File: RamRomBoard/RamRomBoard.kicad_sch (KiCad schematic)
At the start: 84 parts, among them J10 Micro_SD_Card_Det2, J5 Screw_Terminal_01x02, J6 USB_B_Micro, J7 STM32F401, J8 Dual LED Socket, J9 JTAG, SW1 033TBVSA, SW2 SW_Push, U1 74LVC125, U10 74AHC1G14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

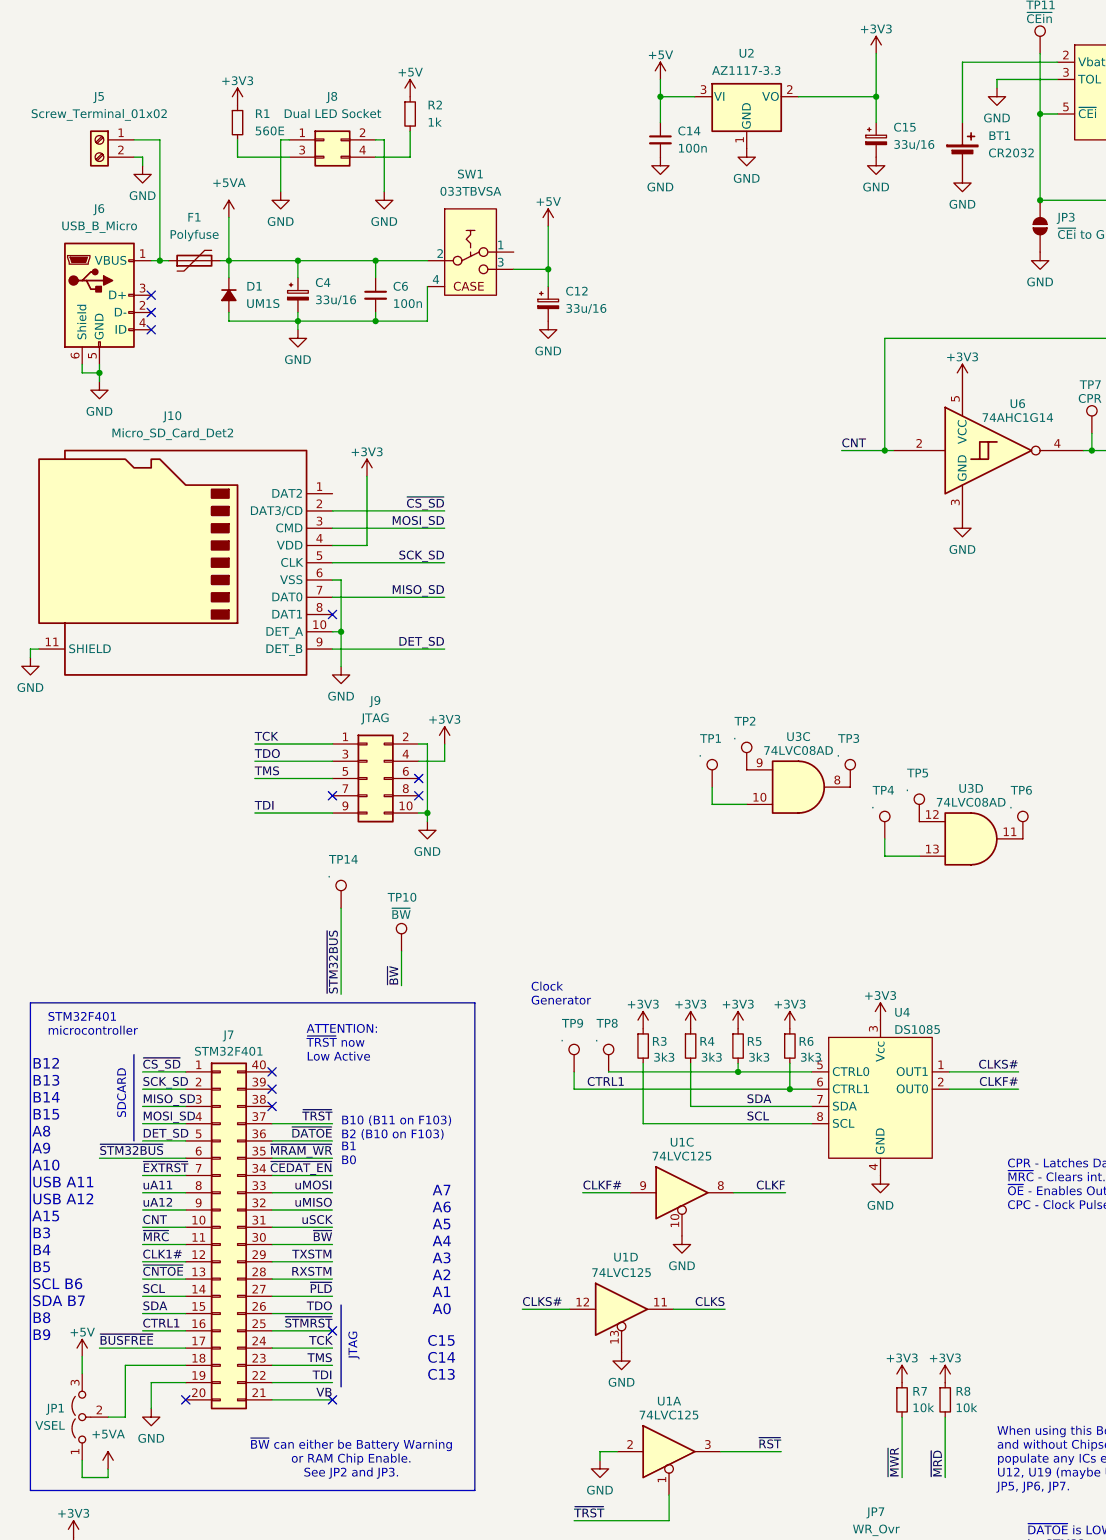
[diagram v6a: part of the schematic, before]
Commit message: first boards manufactured
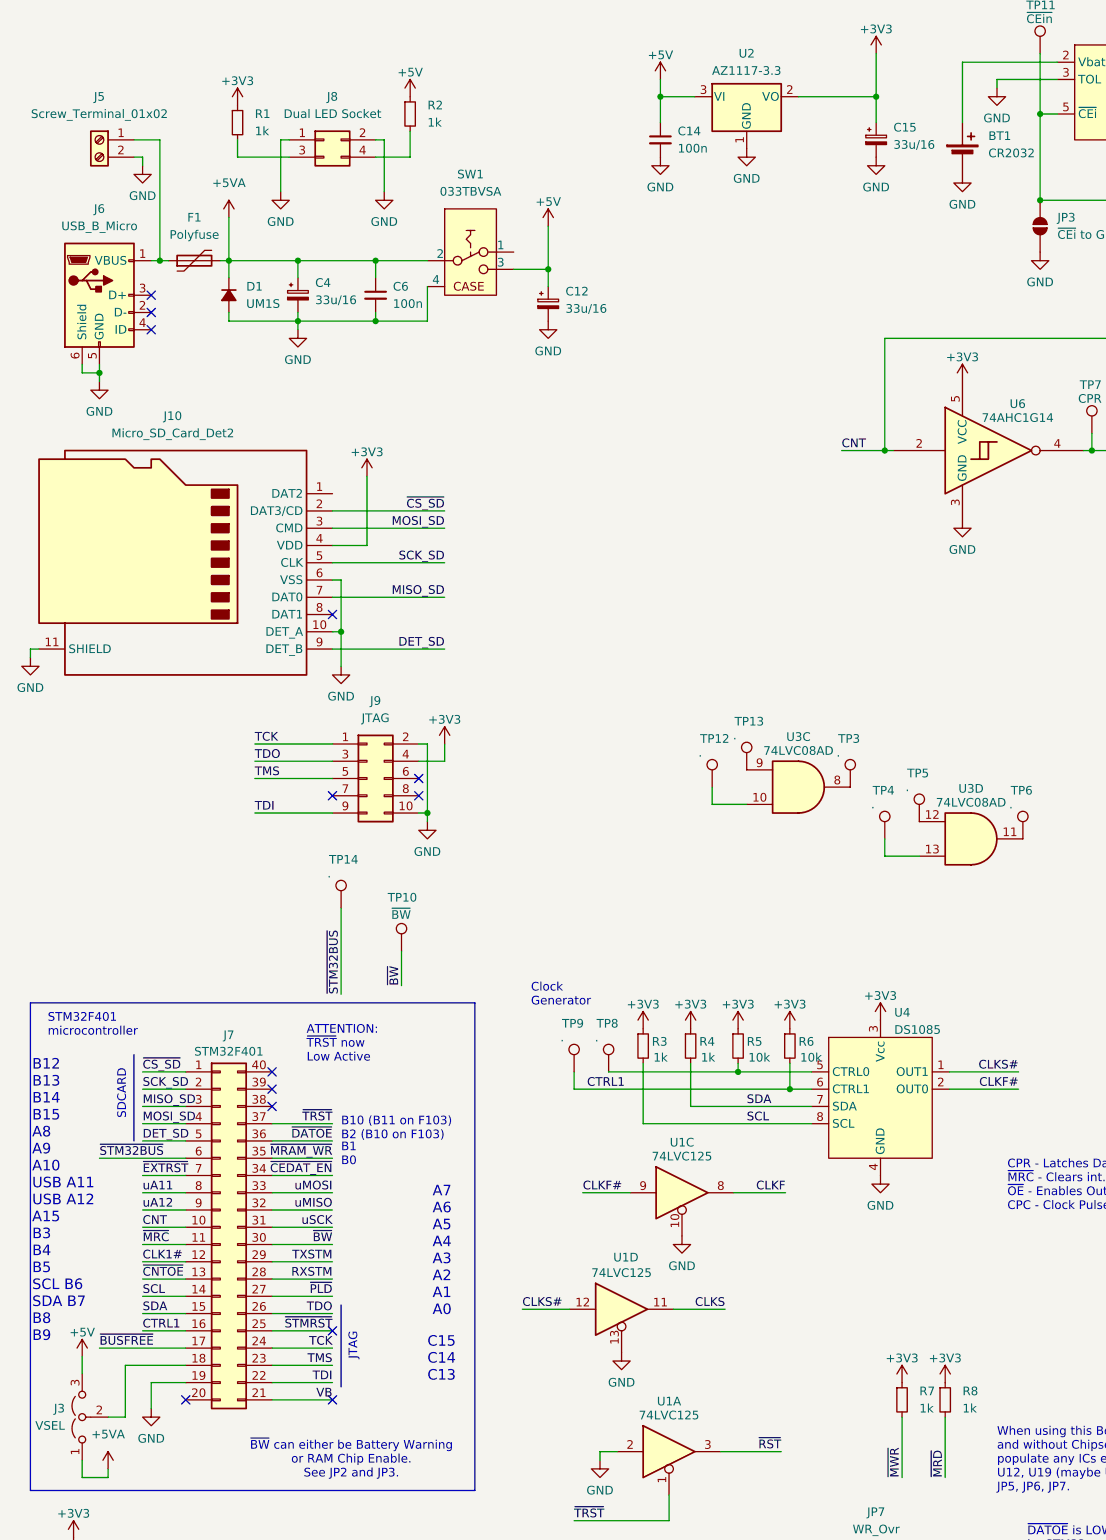
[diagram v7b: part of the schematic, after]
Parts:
- J3: renamed from JP1; now in the parts list
- R1: value 560E -> 1k
- R3, R4: value 3k3 -> 1k
- R5, R6: value 3k3 -> 10k
- R7, R8: value 10k -> 1k
- renumbered TP1 to TP12, TP2 to TP13
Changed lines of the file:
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@@
 			)
 		)
-		(property "Value" "3k3"
+		(property "Value" "1k"
 			(at 113.8936 168.0722 0)
 			(effects
@@
 			)
 		)
-		(property "Value" "3k3"
+		(property "Value" "1k"
 			(at 106.9086 168.0722 0)
 			(effects
@@
 			)
 		)
-		(property "Value" "3k3"
+		(property "Value" "10k"
 			(at 128.4986 168.0722 0)
 			(effects
@@
 		(on_board yes)
 		(dnp no)
-		(property "Reference" "TP1"
+		(property "Reference" "TP12"
 			(at 113.792 121.158 0)
 			(effects
@@
 			(project "RamRomBoard"
 				(path "/2eaa3998-c9cb-43b1-9b23-df656c8158b0"
-					(reference "TP1")
+					(reference "TP12")
 					(unit 1)
 				)
@@
 		(fields_autoplaced yes)
 		(property "Reference" "R8"
-			(at 151.3586 217.2279 0)
+			(at 152.4 217.1699 0)
 			(effects
 				(font
@@
 			)
 		)
-		(property "Value" "10k"
-			(at 151.3586 219.6521 0)
+		(property "Value" "1k"
+			(at 152.4 219.7099 0)
 			(effects
 				(font
@@
 		(unit 1)
 		(exclude_from_sim yes)
-		(in_bom no)
+		(in_bom yes)
 		(on_board yes)
 		(dnp no)
 		(fields_autoplaced yes)
-		(property "Reference" "JP1"
+		(property "Reference" "J3"
 			(at 20.32 219.7099 90)
 			(effects
@@
 			(project ""
 				(path "/2eaa3998-c9cb-43b1-9b23-df656c8158b0"
-					(reference "JP1")
+					(reference "J3")
 					(unit 1)
 				)
@@
 			)
 		)
-		(property "Value" "560E"
+		(property "Value" "1k"
 			(at 48.26 31.7499 0)
 			(effects
@@
 			)
 		)
-		(property "Value" "3k3"
+		(property "Value" "10k"
 			(at 120.8786 168.0722 0)
 			(effects
@@
 		(on_board yes)
 		(dnp no)
-		(property "Reference" "TP2"
+		(property "Reference" "TP13"
 			(at 118.872 118.618 0)
 			(effects
@@
 			(project "RamRomBoard"
 				(path "/2eaa3998-c9cb-43b1-9b23-df656c8158b0"
-					(reference "TP2")
+					(reference "TP13")
 					(unit 1)
 				)
@@
 		(fields_autoplaced yes)
 		(property "Reference" "R7"
-			(at 145.0086 217.2279 0)
+			(at 146.05 217.1699 0)
 			(effects
 				(font
@@
 			)
 		)
-		(property "Value" "10k"
-			(at 145.0086 219.6521 0)
+		(property "Value" "1k"
+			(at 146.05 219.7099 0)
 			(effects
 				(font
